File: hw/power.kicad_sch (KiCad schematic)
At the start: 36 parts, among them J1 TYPE-C-31-M-13C, J2 Conn_01x02, U2 NPM1300-QEAA-R

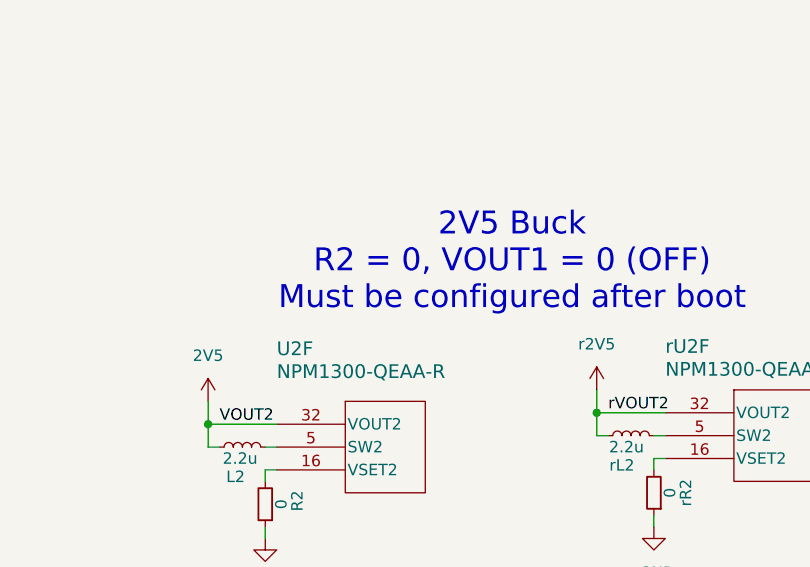
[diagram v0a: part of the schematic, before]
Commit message: Place FPGA
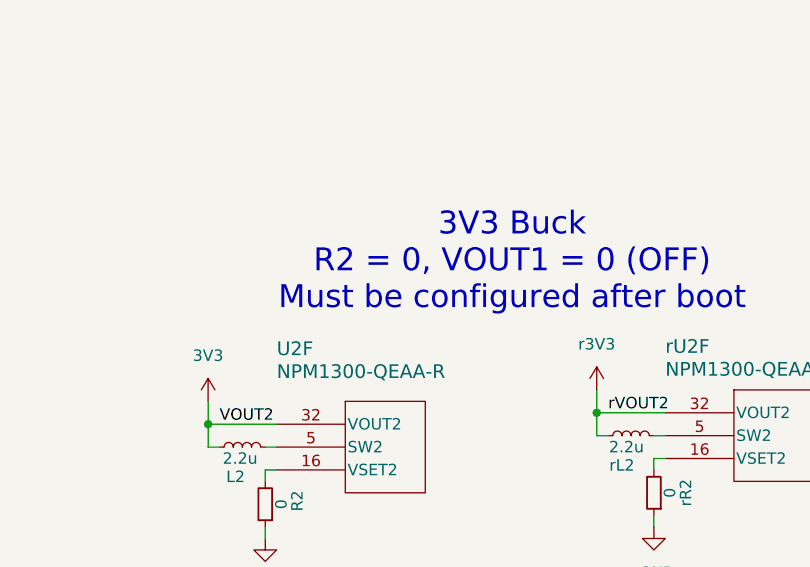
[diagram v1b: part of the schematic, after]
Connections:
- net 2V5 renamed 3V3
- net r2V5 renamed r3V3
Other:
- note added: "3V3 Buck R2 = 0, VOUT1 = 0 (OFF) Must be configured after boot"
- note removed: "2V5 Buck R2 = 0, VOUT1 = 0 (OFF) Must be configured after boot"
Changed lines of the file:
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@@
 		)
 	)
-	(text "2V5 Buck\nR2 = 0, VOUT1 = 0 (OFF)\nMust be configured after boot"
+	(text "3V3 Buck\nR2 = 0, VOUT1 = 0 (OFF)\nMust be configured after boot"
 		(exclude_from_sim no)
 		(at 169.672 126.746 0)
@@
 	)
 	(symbol
+		(lib_id "Alidade:r2V5")
+		(at 179.07 140.97 0)
+		(unit 1)
+		(exclude_from_sim no)
+		(in_bom yes)
+		(on_board yes)
+		(dnp no)
+		(fields_autoplaced yes)
+		(property "Reference" "#r3V3_01"
+			(at 179.07 144.78 0)
+			(effects
+				(font
+					(size 1.27 1.27)
+				)
+				(hide yes)
+			)
+		)
+		(property "Value" "r3V3"
+			(at 179.07 135.89 0)
+			(effects
+				(font
+					(size 1.27 1.27)
+				)
+			)
+		)
+		(property "Footprint" ""
+			(at 179.07 140.97 0)
+			(effects
+				(font
+					(size 1.27 1.27)
+				)
+				(hide yes)
+			)
+		)
+		(property "Datasheet" ""
+			(at 179.07 140.97 0)
+			(effects
+				(font
+					(size 1.27 1.27)
+				)
+				(hide yes)
+			)
+		)
+		(property "Description" ""
+			(at 179.07 140.97 0)
+			(effects
+				(font
+					(size 1.27 1.27)
+				)
+			)
+		)
+		(pin "1"
+		)
+		(instances
+			(project ""
+				(path "/4cc5d416-57f5-4147-8183-e03ae6b1198a/29a12dcc-0491-44a2-8290-cbef7c573a8c"
+					(reference "#r3V3_01")
+					(unit 1)
+				)
+			)
+		)
+	)
+	(symbol
 		(lib_id "Alidade:C")
 		(at 257.81 148.59 0)
@@
 	)
 	(symbol
+		(lib_id "Alidade:3V3")
+		(at 135.89 142.24 0)
+		(unit 1)
+		(exclude_from_sim no)
+		(in_bom yes)
+		(on_board yes)
+		(dnp no)
+		(fields_autoplaced yes)
+		(property "Reference" "#3V3_01"
+			(at 135.89 146.05 0)
+			(effects
+				(font
+					(size 1.27 1.27)
+				)
+				(hide yes)
+			)
+		)
+		(property "Value" "3V3"
+			(at 135.89 137.16 0)
+			(effects
+				(font
+					(size 1.27 1.27)
+				)
+			)
+		)
+		(property "Footprint" ""
+			(at 135.89 142.24 0)
+			(effects
+				(font
+					(size 1.27 1.27)
+				)
+				(hide yes)
+			)
+		)
+		(property "Datasheet" ""
+			(at 135.89 142.24 0)
+			(effects
+				(font
+					(size 1.27 1.27)
+				)
+				(hide yes)
+			)
+		)
+		(property "Description" ""
+			(at 135.89 142.24 0)
+			(effects
+				(font
+					(size 1.27 1.27)
+				)
+			)
+		)
+		(pin "1"
+		)
+		(instances
+			(project ""
+				(path "/4cc5d416-57f5-4147-8183-e03ae6b1198a/29a12dcc-0491-44a2-8290-cbef7c573a8c"
+					(reference "#3V3_01")
+					(unit 1)
+				)
+			)
+		)
+	)
+	(symbol
 		(lib_id "Alidade:C")
 		(at 295.91 148.59 0)
@@
 	)
 	(symbol
-		(lib_id "Alidade:r2V5")
-		(at 179.07 140.97 0)
-		(unit 1)
-		(exclude_from_sim no)
-		(in_bom yes)
-		(on_board yes)
-		(dnp no)
-		(fields_autoplaced yes)
-		(property "Reference" "#r2V5_01"
-			(at 179.07 144.78 0)
-			(effects
-				(font
-					(size 1.27 1.27)
-				)
-				(hide yes)
-			)
-		)
-		(property "Value" "r2V5"
-			(at 179.07 135.89 0)
-			(effects
-				(font
-					(size 1.27 1.27)
-				)
-			)
-		)
-		(property "Footprint" ""
-			(at 179.07 140.97 0)
-			(effects
-				(font
-					(size 1.27 1.27)
-				)
-				(hide yes)
-			)
-		)
-		(property "Datasheet" ""
-			(at 179.07 140.97 0)
-			(effects
-				(font
-					(size 1.27 1.27)
-				)
-				(hide yes)
-			)
-		)
-		(property "Description" ""
-			(at 179.07 140.97 0)
-			(effects
-				(font
-					(size 1.27 1.27)
-				)
-			)
-		)
-		(pin "1"
-		)
-		(instances
-			(project ""
-				(path "/4cc5d416-57f5-4147-8183-e03ae6b1198a/29a12dcc-0491-44a2-8290-cbef7c573a8c"
-					(reference "#r2V5_01")
-					(unit 1)
-				)
-			)
-		)
-	)
-	(symbol
 		(lib_id "Alidade:L")
 		(at 85.09 142.24 90)
@@
 					(unit 1)
 				)
-			)
-		)
-	)
-	(symbol
-		(lib_id "Alidade:2V5")
-		(at 135.89 142.24 0)
-		(unit 1)
-		(exclude_from_sim no)
-		(in_bom yes)
-		(on_board yes)
-		(dnp no)
-		(fields_autoplaced yes)
-		(property "Reference" "#2V5_01"
-			(at 135.89 146.05 0)
-			(effects
-				(font
-					(size 1.27 1.27)
-				)
-				(hide yes)
-			)
-		)
-		(property "Value" "2V5"
-			(at 135.89 137.16 0)
-			(effects
-				(font
-					(size 1.27 1.27)
-				)
-			)
-		)
-		(property "Footprint" ""
-			(at 135.89 142.24 0)
-			(effects
-				(font
-					(size 1.27 1.27)
-				)
-				(hide yes)
-			)
-		)
-		(property "Datasheet" ""
-			(at 135.89 142.24 0)
-			(effects
-				(font
-					(size 1.27 1.27)
-				)
-				(hide yes)
-			)
-		)
-		(property "Description" ""
-			(at 135.89 142.24 0)
-			(effects
-				(font
-					(size 1.27 1.27)
-				)
-			)
-		)
-		(pin "1"
-		)
-		(instances
-			(project ""
-				(path "/4cc5d416-57f5-4147-8183-e03ae6b1198a/29a12dcc-0491-44a2-8290-cbef7c573a8c"
-					(reference "#2V5_01")
-					(unit 1)
-				)

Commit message: Sheet pins
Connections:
- net SCL renamed PMICSCL
- net SDA renamed PMICSDA
- net rSCL renamed rPMICSCL
- net rSDA renamed rPMICSDA
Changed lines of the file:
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@@
 		)
 	)
-	(hierarchical_label "SCL"
+	(hierarchical_label "PMICSCL"
 		(shape input)
 		(at 219.71 243.84 180)
@@
 		)
 	)
-	(hierarchical_label "rSCL"
+	(hierarchical_label "rPMICSCL"
 		(shape input)
 		(at 264.16 243.84 180)
@@
 		)
 	)
-	(hierarchical_label "SDA"
+	(hierarchical_label "PMICSDA"
 		(shape bidirectional)
 		(at 219.71 241.3 180)
@@
 		)
 	)
-	(hierarchical_label "rSDA"
+	(hierarchical_label "rPMICSDA"
 		(shape bidirectional)
 		(at 264.16 241.3 180)
